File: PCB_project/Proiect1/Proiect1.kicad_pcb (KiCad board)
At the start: 2 copper layers, 40 x 40 mm, 38 parts, among them J1 OUT, J3 +25V, J4 GND, Q1 BC846, Q10 BC846, Q11 BC846, Q12 BC856, Q13 BC856, Q2 BC856, Q3 BC856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

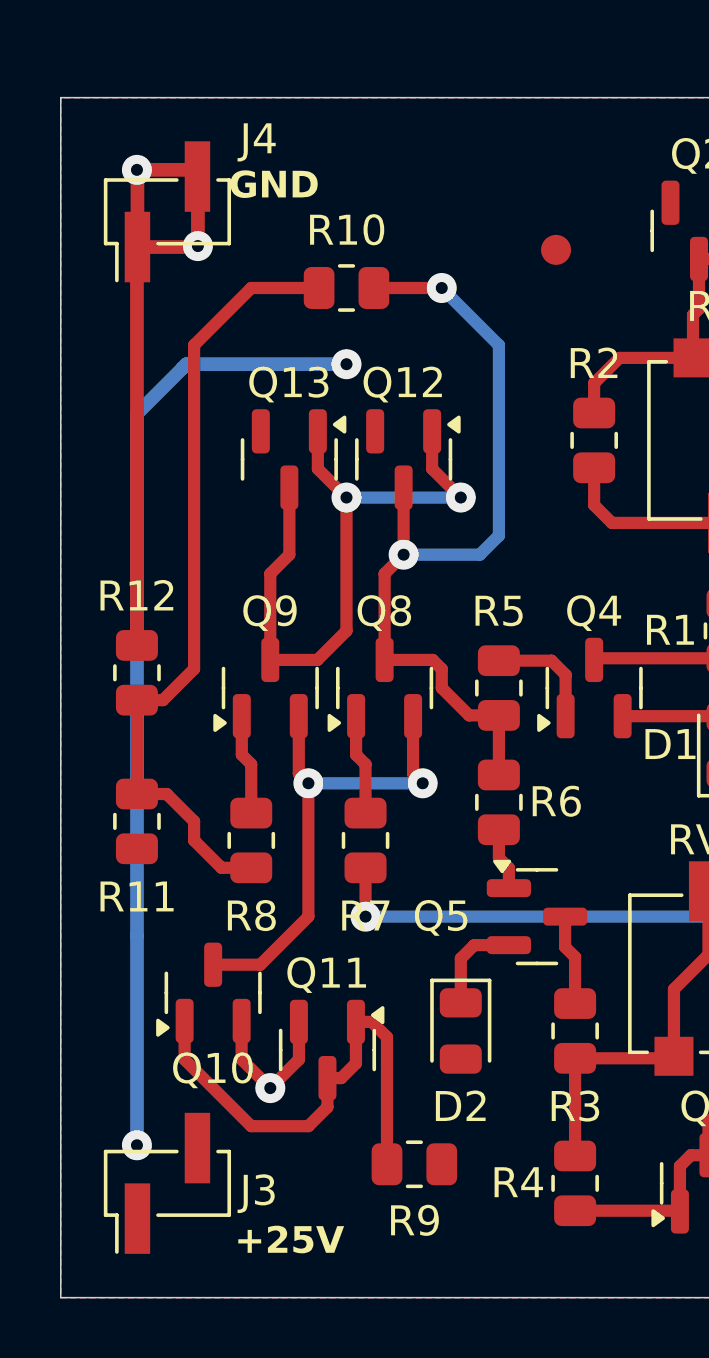
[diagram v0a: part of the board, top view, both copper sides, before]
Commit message: Changed reference designators J3, J4 to J2, J3
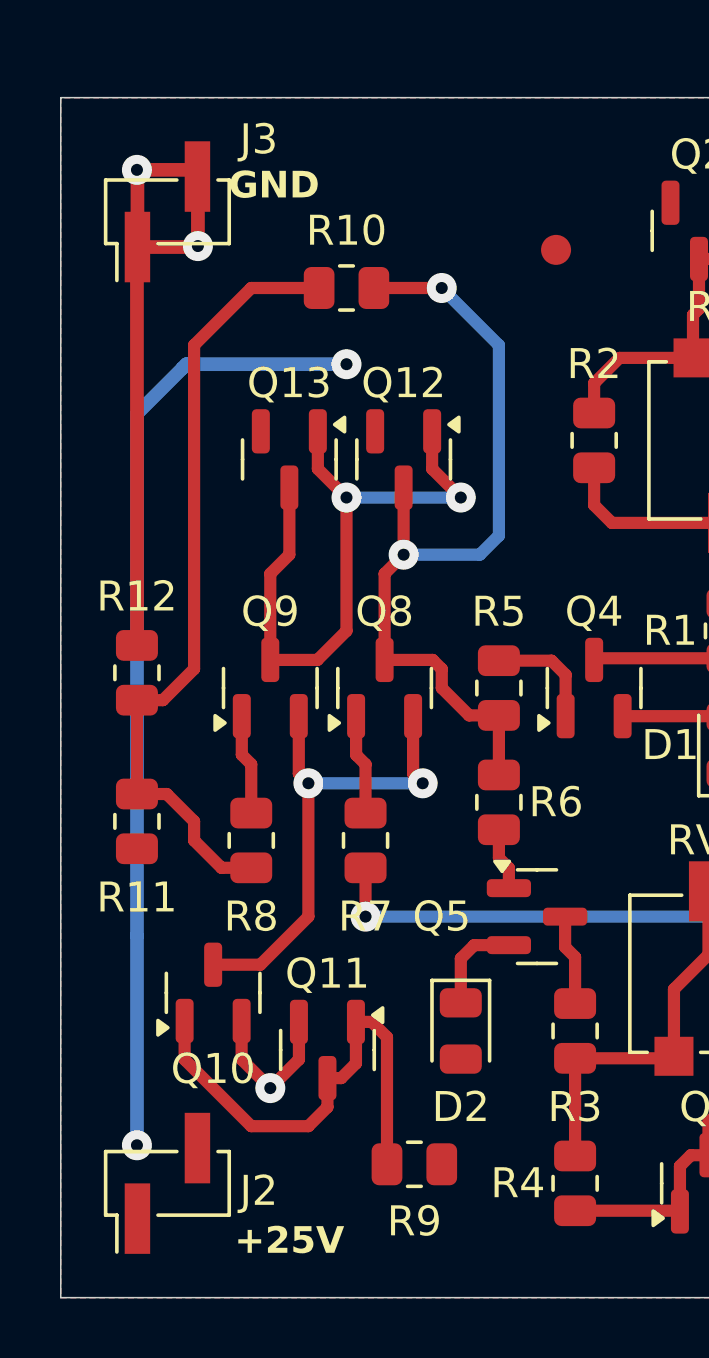
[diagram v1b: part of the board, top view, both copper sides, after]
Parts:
- renumbered J3 to J2, J4 to J3
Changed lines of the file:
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@@
 		(descr "surface-mounted straight pin header, 1x02, 2.00mm pitch, single row, style 1 (pin 1 left)")
 		(tags "Surface mounted pin header SMD 1x02 2.00mm single row style1 pin1 left")
-		(property "Reference" "J3"
+		(property "Reference" "J2"
 			(at -0.254 3.048 0)
 			(layer "F.SilkS")
@@
 		(descr "surface-mounted straight pin header, 1x02, 2.00mm pitch, single row, style 1 (pin 1 left)")
 		(tags "Surface mounted pin header SMD 1x02 2.00mm single row style1 pin1 left")
-		(property "Reference" "J4"
+		(property "Reference" "J3"
 			(at 2.413 3.048 0)
 			(layer "F.SilkS")

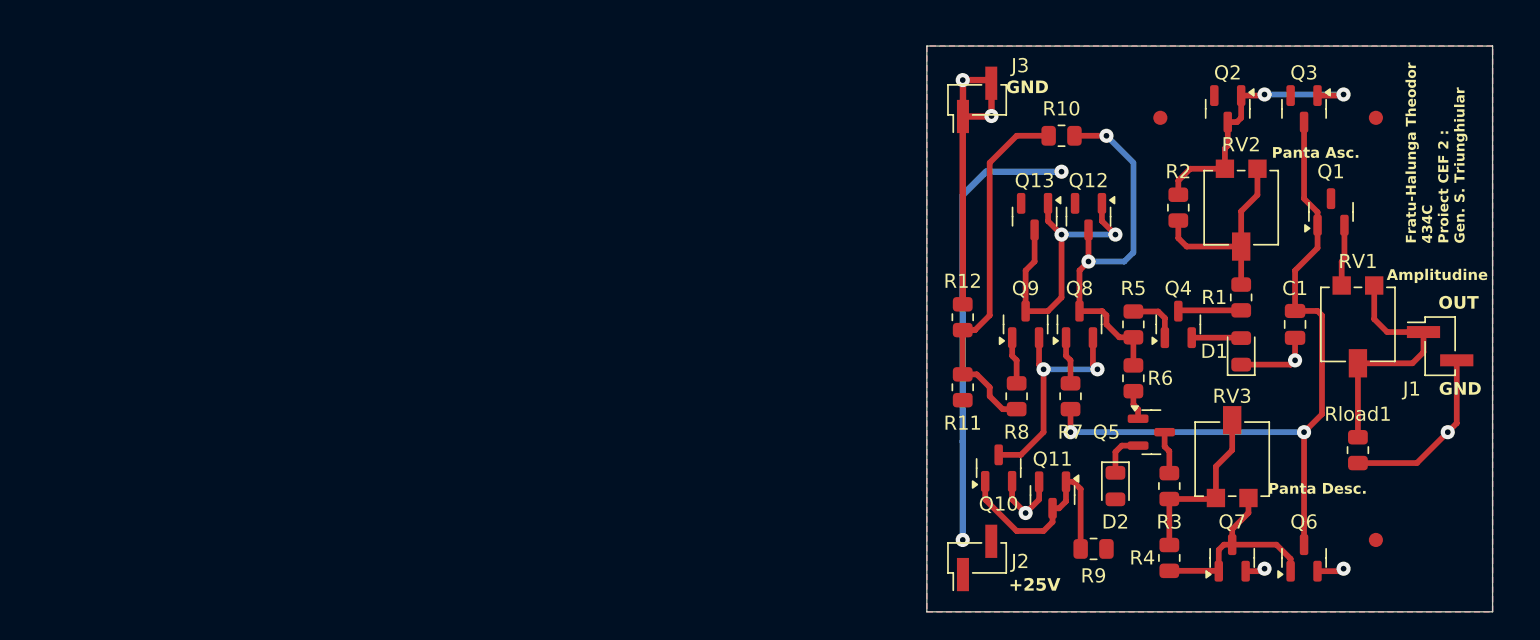
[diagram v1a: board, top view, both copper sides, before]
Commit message: Added Drill Table and simple stackup table
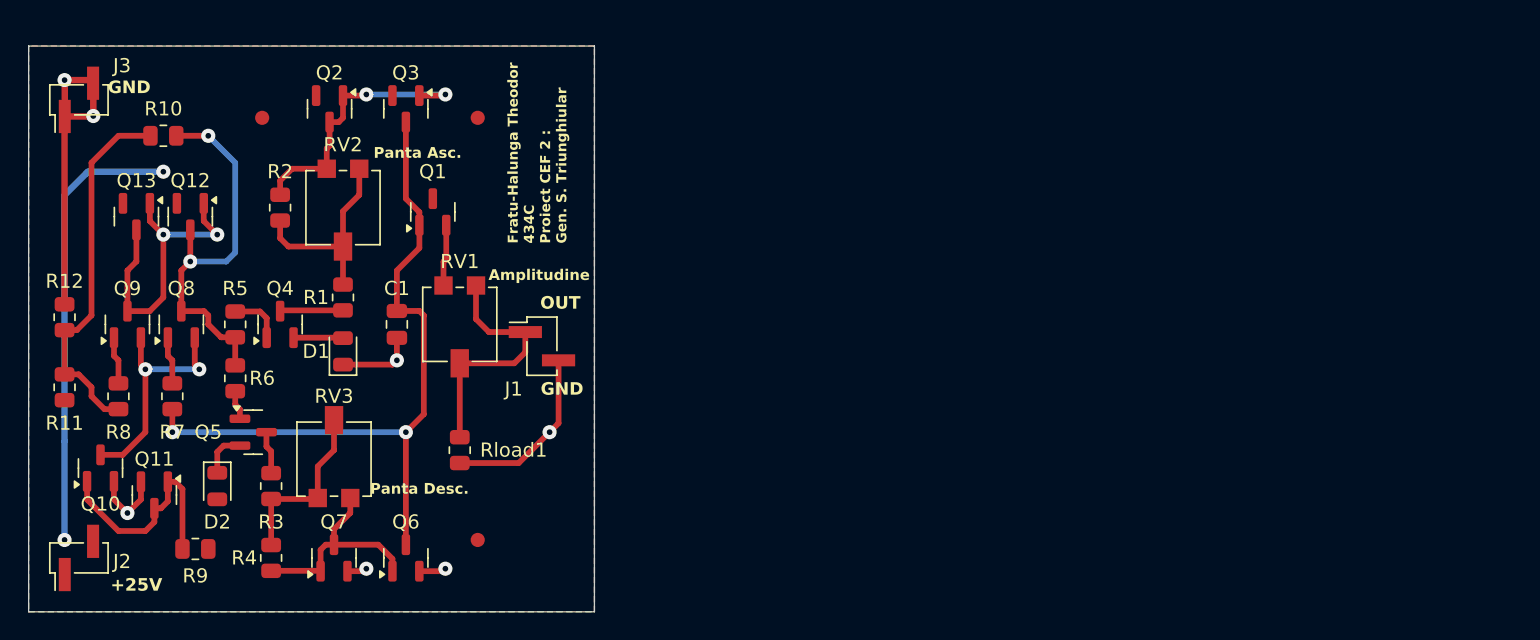
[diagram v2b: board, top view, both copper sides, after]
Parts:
- moved D2 63.5 mm to (74.8, 106.1)
- moved J2 63.5 mm to (65.1, 111.2)
- moved J3 63.5 mm to (65.1, 78.8)
- moved Q10 63.5 mm to (66.6, 104.8)
- moved Q9 63.5 mm to (68.5, 94.7)
- moved R3 63.5 mm to (78.6, 106.1)
- moved R4 63.5 mm to (78.6, 111.2)
- moved C1 63.5 mm to (87.5, 94.7)
- moved D1 63.5 mm to (83.7, 96.6)
- moved FID2 63.5 mm to (93.2, 80.1)
- moved FID3 63.5 mm to (93.2, 109.9)
- moved Q12 63.5 mm to (72.9, 87.1)
- moved Q13 63.5 mm to (69.1, 87.1)
- moved Q2 63.5 mm to (82.8, 79.4)
- moved Q4 63.5 mm to (79.3, 94.7)
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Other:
- board text added: "0"
- board text added: "0 mm"
- board text added: "0.01 mm"
- board text added: "0.018 mm"
- board text added: "0.02"
- board text added: "1"
- board text added: "1.544 mm"
- board text added: "3.3"
- board text added: "4.5"
- board text added: "B.Cu"
- board text added: "B.Mask"
- board text added: "B.Paste"
- board text added: "B.Silkscreen"
- board text added: "Bottom Silk Screen"
- board text added: "Bottom Solder Mask"
- board text added: "Bottom Solder Paste"
- board text added: "Color"
- board text added: "Dielectric 1"
- board text added: "Epsilon R"
- board text added: "F.Cu"
- board text added: "F.Mask"
- board text added: "F.Paste"
- board text added: "F.Silkscreen"
- board text added: "FR4"
- board text added: "Layer Name"
- board text added: "Loss Tangent"
- board text added: "Material"
- board text added: "Not specified"
- board text added: "Thickness (mm)"
- board text added: "Top Silk Screen"
- board text added: "Top Solder Mask"
- board text added: "Top Solder Paste"
- board text added: "Type"
- board text added: "copper"
- board text added: "core"

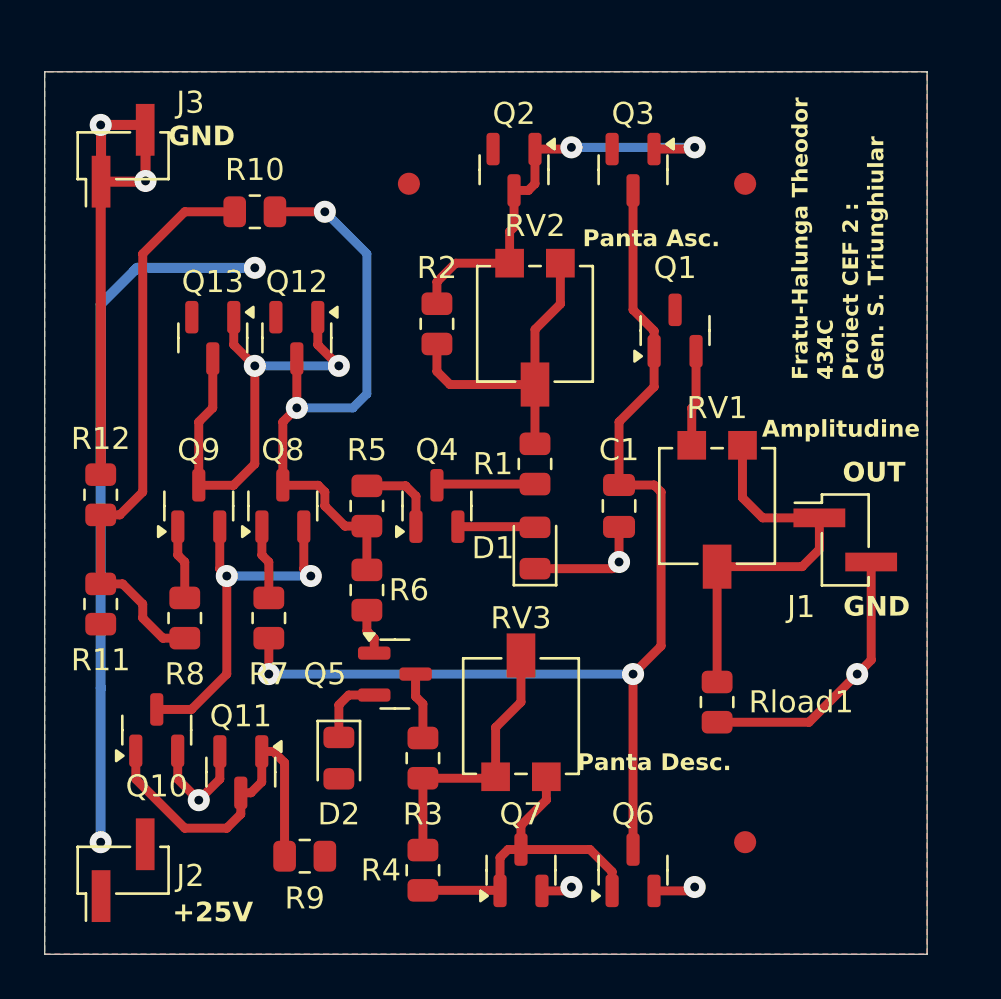
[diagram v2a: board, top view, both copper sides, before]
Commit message: Changed footprints of header pins for Power and Output
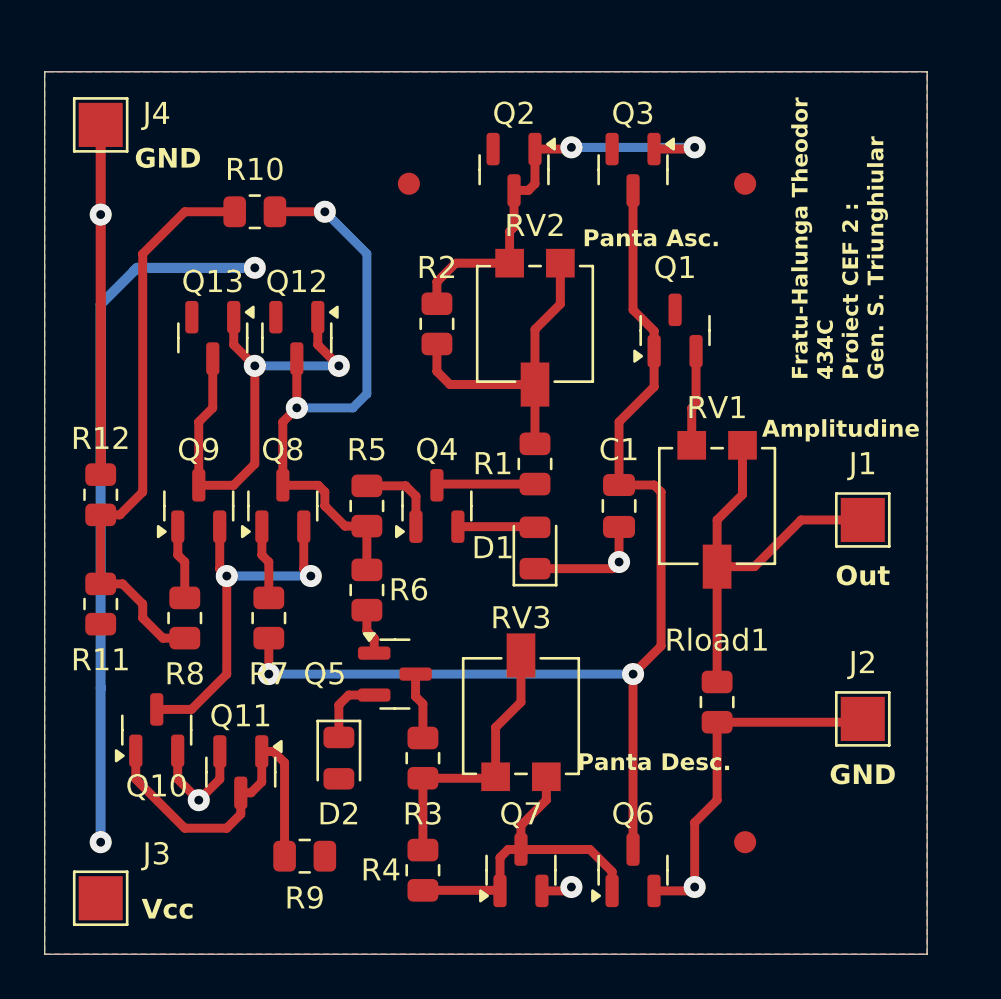
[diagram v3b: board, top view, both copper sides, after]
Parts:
- added J4: GND, TestPoint:TestPoint_Pad_2.0x2.0mm, F.Cu at (64.0, 77.4)
- J1: value OUT -> Out; footprint Connector_PinHeader_2.00mm:PinHeader_1x02_P2.00mm_Vertical_SMD_Pin1Left -> TestPoint:TestPoint_Pad_2.0x2.0mm
- J2: value +25V -> GND; footprint Connector_PinHeader_2.00mm:PinHeader_1x02_P2.00mm_Vertical_SMD_Pin1Left -> TestPoint:TestPoint_Pad_2.0x2.0mm
- J3: value GND -> Vcc; footprint Connector_PinHeader_2.00mm:PinHeader_1x02_P2.00mm_Vertical_SMD_Pin1Left -> TestPoint:TestPoint_Pad_2.0x2.0mm
- moved J2 34.2 mm to (98.6, 104.3), turned to 0 degrees
- moved J3 33.7 mm to (64.0, 112.5), turned to 0 degrees
- moved J1 1.20 mm to (98.6, 95.3)
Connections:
- J2 pad 1: +25V -> GND
- J3 pad 1: GND -> +25V
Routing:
- net GND: track 49.0 -> 44.5 mm, vias 7 -> 5
- net Net-(J1-Pin_1): track 17.9 -> 18.7 mm
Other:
- board text removed: "GND"
